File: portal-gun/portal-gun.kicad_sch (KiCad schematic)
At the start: 8 parts, among them J1 SAO, SW1 SW_Push

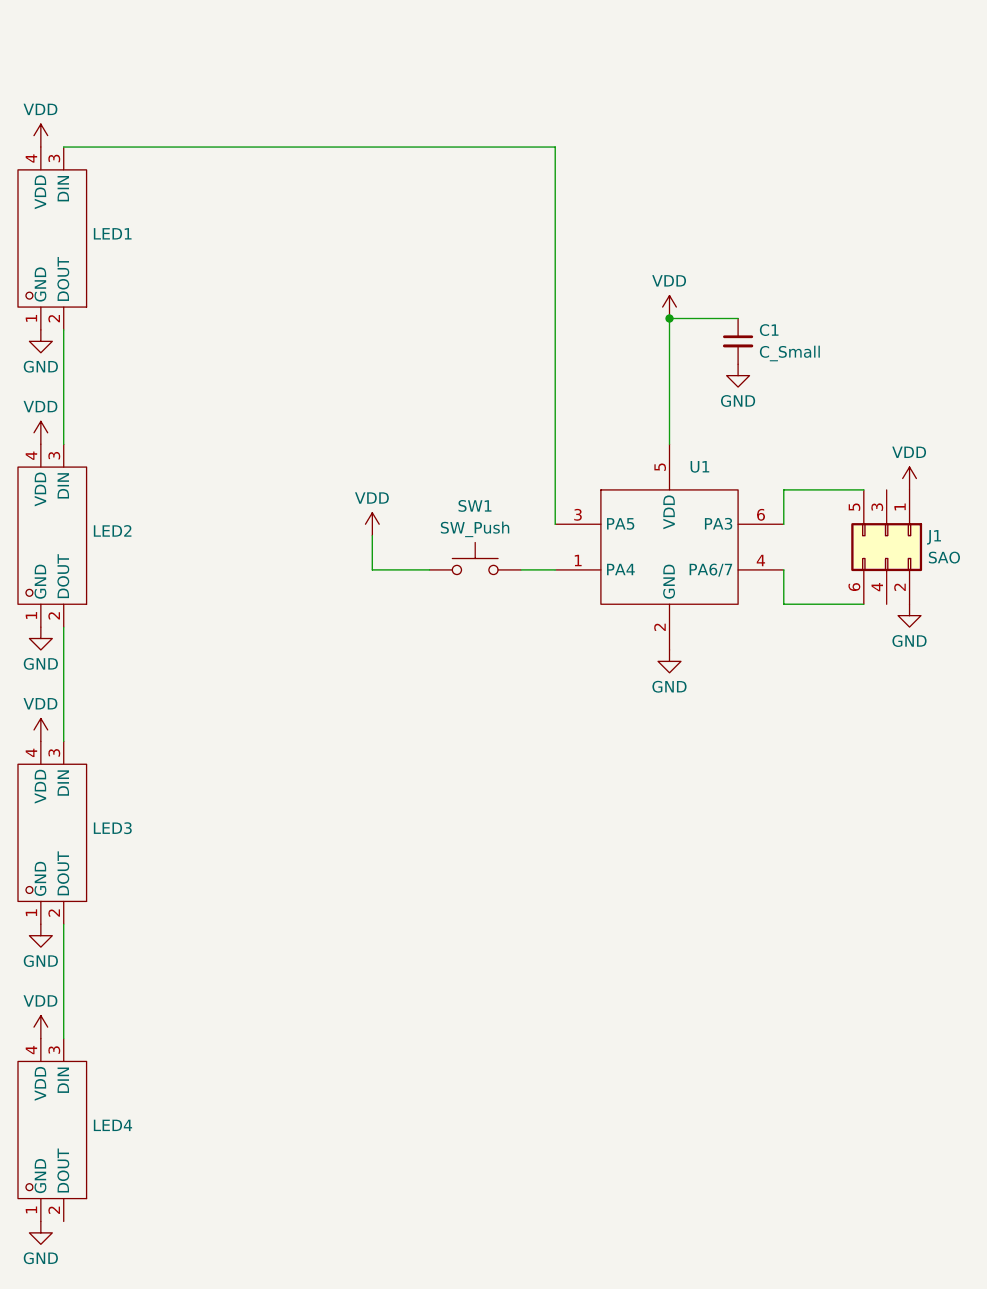
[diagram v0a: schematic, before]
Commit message: added res to pin 6 for output
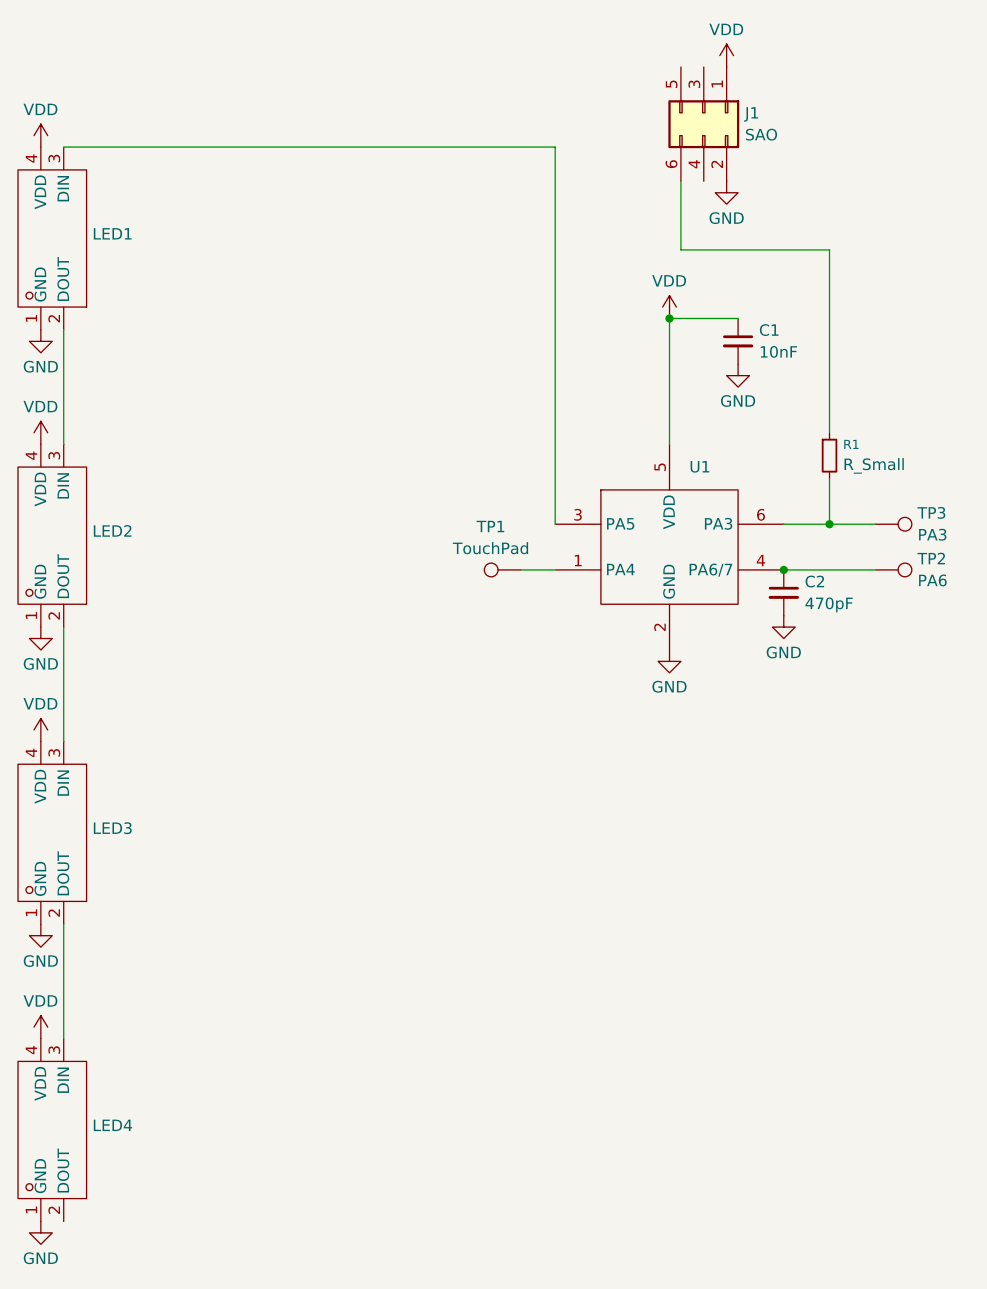
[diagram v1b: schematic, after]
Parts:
- removed SW1: SW_Push, Button_Switch_SMD:SW-SMD_GT-TC050C-H050-L1, symbol Switch:SW_Push
- added C2: 470pF, Capacitor_SMD:C_0603_1608Metric, symbol Device:C_Small
- added R1: R_Small, Resistor_SMD:R_0603_1608Metric, symbol Device:R_Small
- added TP1: TouchPad, TestPoint:TestPoint_Pad_1.0x1.0mm, symbol Connector:TestPoint
- added TP2: PA6, TestPoint:TestPoint_Pad_1.0x1.0mm, symbol Connector:TestPoint
- added TP3: PA3, TestPoint:TestPoint_Pad_1.0x1.0mm, symbol Connector:TestPoint
- C1: value C_Small -> 10nF
- LED1, LED2, LED3, LED4, U1: value ~ -> (none)
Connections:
- net GND: now also C2.2
- net at U1.1 (PA4): now also TP1.1
- net at U1.6 (PA3): now also R1.2, TP3.1; no longer J1.5 (Pin_5)
- net at U1.4 (PA6/7): now also C2.1, TP2.1; no longer J1.6 (Pin_6)
- new net: J1.6 (Pin_6), R1.1
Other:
- moved on the sheet: J1
